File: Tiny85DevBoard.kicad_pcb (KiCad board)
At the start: 2 copper layers, 36.1 x 27.4 mm, 13 parts, among them J1 Screw_Terminal_01x02, J2 AVR-ISP-6, J3 Conn_01x04_Female, J4 Conn_01x04_Female, SW1 SW_SPDT, SW2 Reset, U1 LD1117S33TR_SOT223, U2 ATtiny85-20PU

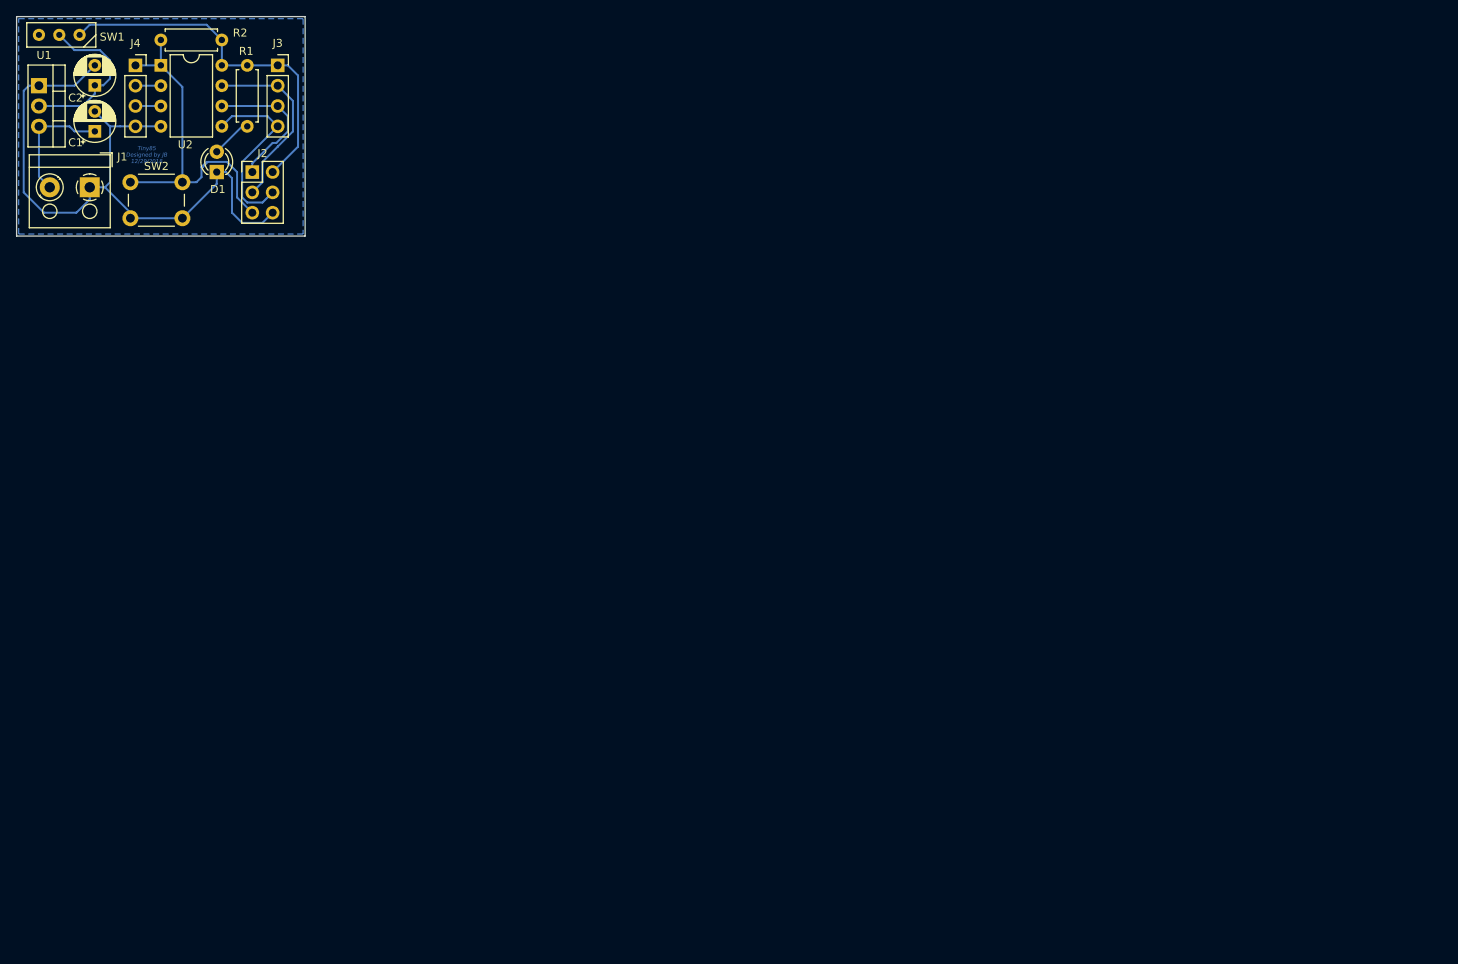
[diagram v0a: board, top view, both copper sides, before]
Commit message: Moved power and added labels.
Moved the power block above the microcontroller and headers so
the headers would be at the sides of the board. Added silkscreen
labels for power, pin names, and header names.
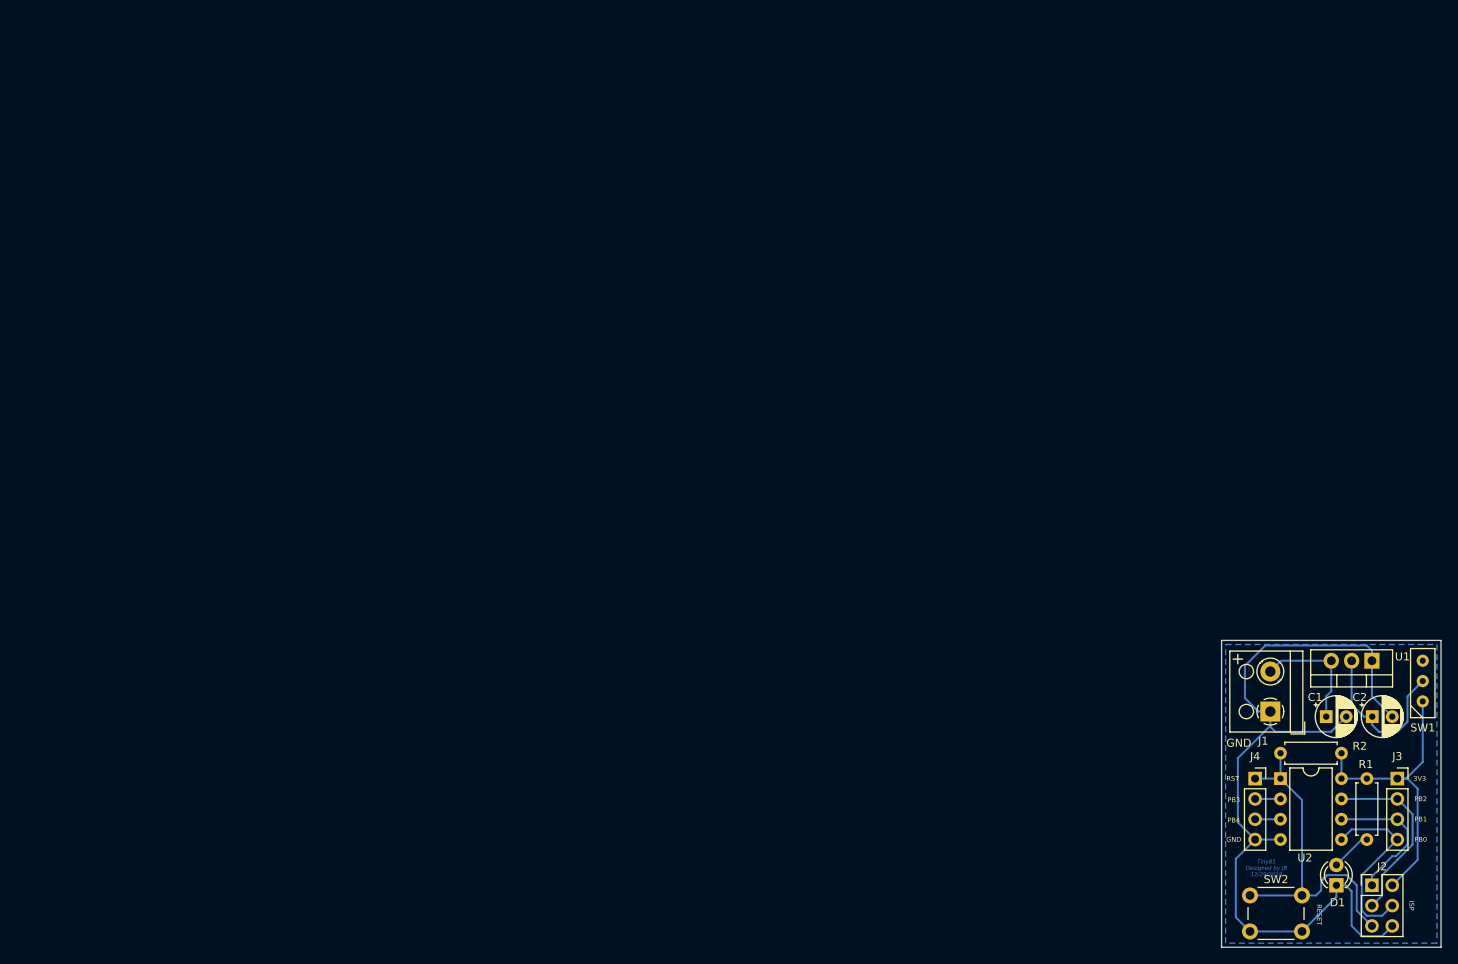
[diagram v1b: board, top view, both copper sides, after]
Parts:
- moved SW1 187.4 mm to (188.2, 98.0), turned to 90 degrees
- moved U1 181.5 mm to (181.9, 93.0), turned to 180 degrees
- moved C2 178.1 mm to (181.9, 99.9), turned to 0 degrees
- moved C1 170.4 mm to (176.1, 99.9), turned to 0 degrees
- moved D1 165.9 mm to (177.4, 121.0)
- moved J2 165.9 mm to (181.9, 121.0)
- moved R1 165.9 mm to (181.2, 107.7)
- moved R2 165.9 mm to (170.4, 104.5)
- moved SW2 165.9 mm to (166.6, 122.3)
- moved U2 165.9 mm to (170.4, 107.7)
- moved J3 165.9 mm to (185.0, 107.7)
- moved J4 165.9 mm to (167.3, 107.7)
- moved J1 161.5 mm to (169.2, 99.3), turned to 90 degrees
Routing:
- net GNDPWR: track 85.1 -> 107.5 mm
- net +3V3: track 45.7 -> 38.2 mm
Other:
- board size 36.1 x 27.4 mm -> 27.4 x 38.4 mm
- board text added: "+"
- board text added: "3V3"
- board text added: "GND"
- board text added: "ISP"
- board text added: "PB0"
- board text added: "PB1"
- board text added: "PB2"
- board text added: "PB3"
- board text added: "PB4"
- board text added: "RESET"
- board text added: "RST"

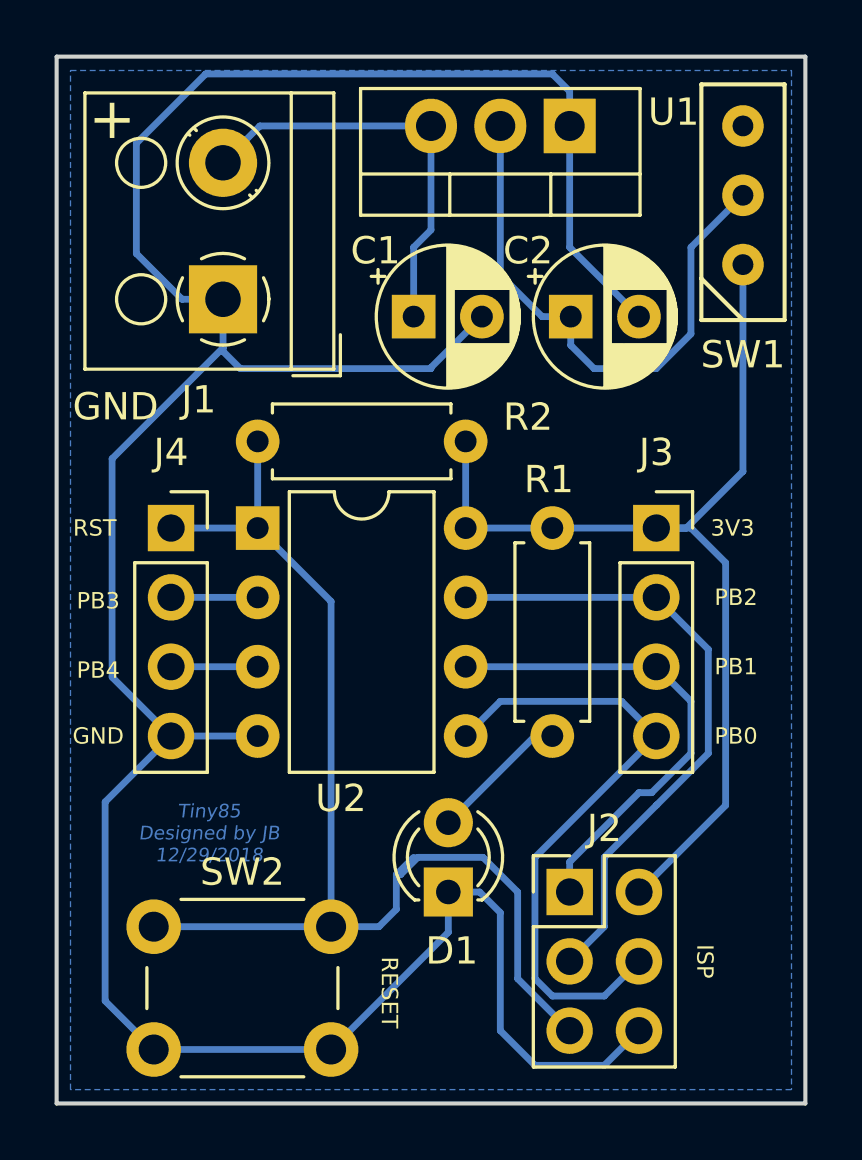
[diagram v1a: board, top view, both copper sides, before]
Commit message: Moved reset switch closer to ATTiny.
There was dead space between the reset switch and the MCU. Moved
the reset switch to eliminate this space.
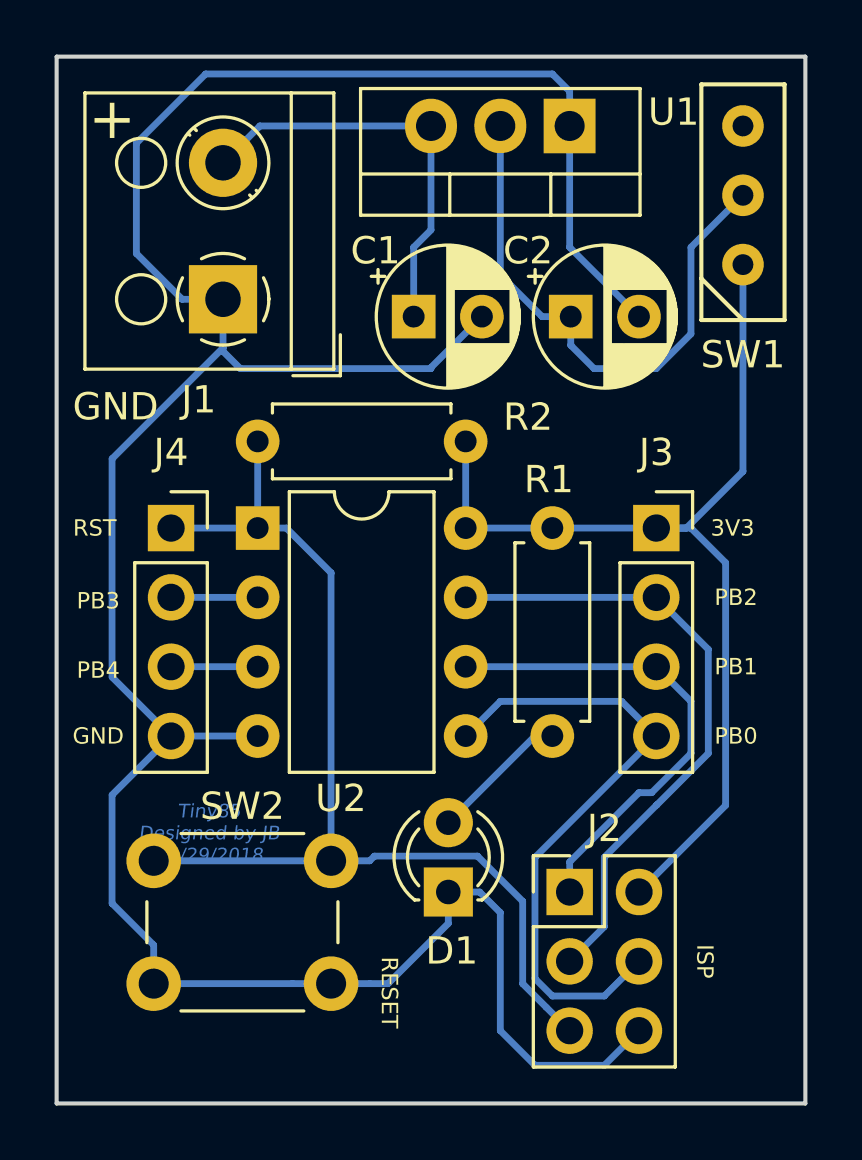
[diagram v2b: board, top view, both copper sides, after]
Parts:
- moved SW2 2.41 mm to (166.6, 119.9)
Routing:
- net GNDPWR: track 107.5 -> 103.0 mm
- net /RESET: track 44.5 -> 40.0 mm
- removed copper zone on B.Cu, net GNDPWR

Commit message: Tightened board, rotated ISP header.
Eliminated dead spaces between components in the power section.
Rotated the ISP header to make it easier to plug in.
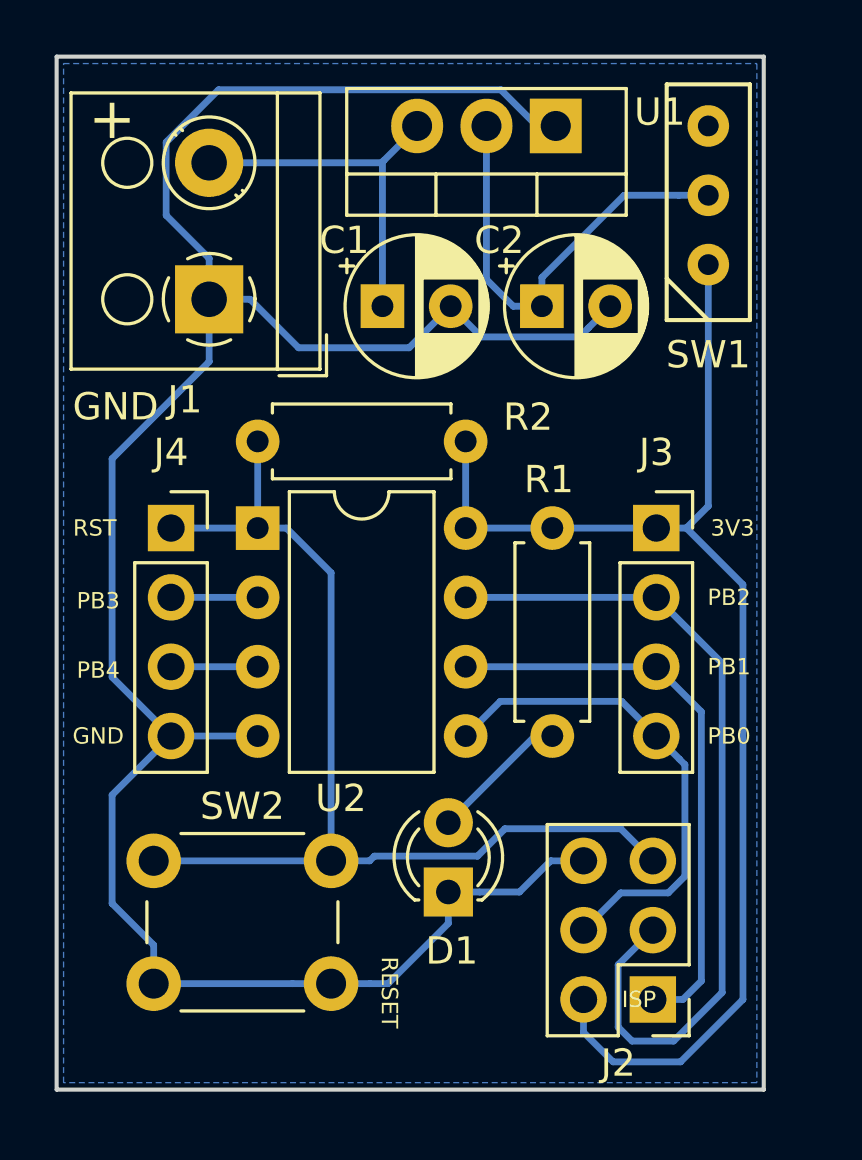
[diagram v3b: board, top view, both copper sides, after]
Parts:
- moved J2 4.98 mm to (184.9, 125.0), turned to 180 degrees
- moved SW1 1.27 mm to (186.9, 98.0)
- moved C1 1.20 mm to (175.0, 99.6)
- moved C2 1.12 mm to (180.8, 99.6)
- moved U1 0.51 mm to (181.4, 93.0)
- moved J1 0.51 mm to (168.7, 99.3)
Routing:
- net GNDPWR: track 103.0 -> 89.4 mm
- net +3V3: track 38.2 -> 47.8 mm
- net /SCK: track 23.2 -> 31.3 mm
- net /MOSI: track 23.4 -> 18.1 mm
- net Net-(C2-Pad1): track 20.9 -> 16.5 mm
- net /MISO: track 17.9 -> 21.2 mm
- net Net-(C1-Pad1): track 15.4 -> 13.6 mm
- added copper zone on B.Cu, net GNDPWR
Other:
- board size 27.4 x 38.4 mm -> 25.9 x 37.8 mm
- board text removed: "Tiny85 Designed by JB 12/29/2018"

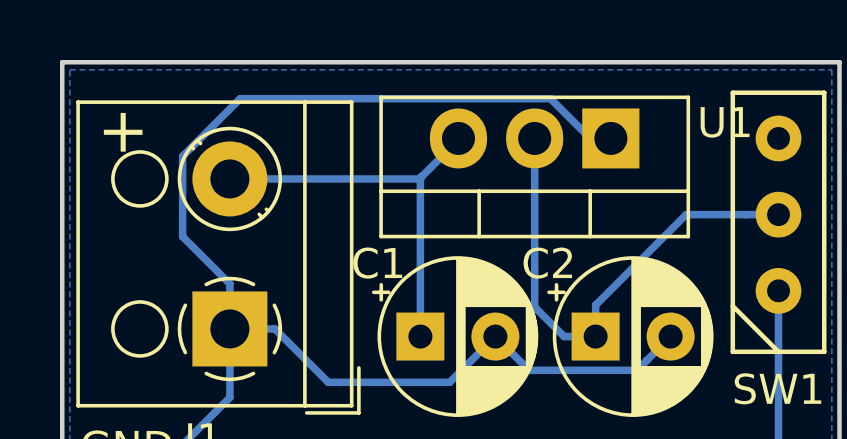
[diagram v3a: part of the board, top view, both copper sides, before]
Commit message: Fine-tuned trace placement.
Moved some ground traces so that they would be within the ground
plane.
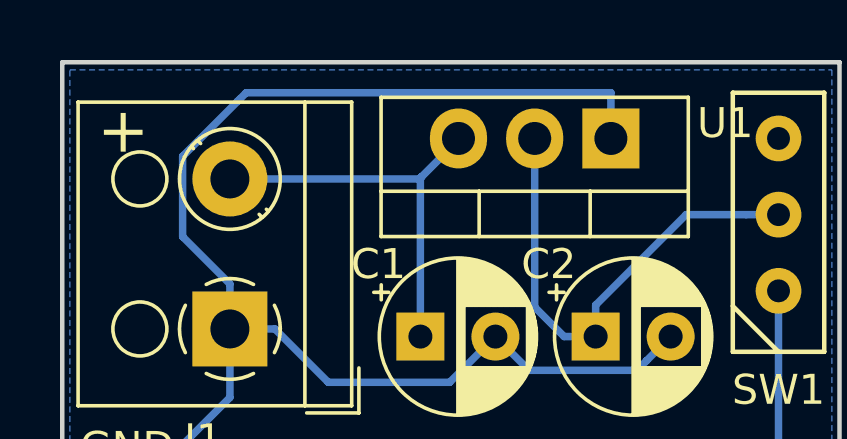
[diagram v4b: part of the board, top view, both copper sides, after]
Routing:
- net GNDPWR: track 89.4 -> 91.3 mm
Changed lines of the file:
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@@
     (thickness 1.6)
     (drawings 16)
-    (tracks 97)
+    (tracks 99)
     (zones 0)
     (modules 13)
@@
     (visible_elements FFFFFF7F)
     (pcbplotparams
-      (layerselection 0x01000_fffffffe)
+      (layerselection 0x01020_fffffffe)
       (usegerberextensions false)
       (usegerberattributes false)
@@
   (segment (start 178.631001 100.693001) (end 182.222999 100.693001) (width 0.25) (layer B.Cu) (net 4))
   (segment (start 177.506 99.568) (end 178.631001 100.693001) (width 0.25) (layer B.Cu) (net 4))
+  (segment (start 181.356 92.964) (end 180.670171 92.964) (width 0.25) (layer B.Cu) (net 4))
+  (segment (start 168.656 97.814) (end 168.656 99.314) (width 0.25) (layer B.Cu) (net 4))
   (segment (start 167.080999 96.238999) (end 168.656 97.814) (width 0.25) (layer B.Cu) (net 4))
-  (segment (start 168.656 97.814) (end 168.656 99.314) (width 0.25) (layer B.Cu) (net 4))
   (segment (start 167.080999 93.557999) (end 167.080999 96.238999) (width 0.25) (layer B.Cu) (net 4))
-  (segment (start 179.345161 91.63899) (end 169.000008 91.63899) (width 0.25) (layer B.Cu) (net 4))
-  (segment (start 180.670171 92.964) (end 179.345161 91.63899) (width 0.25) (layer B.Cu) (net 4))
-  (segment (start 169.000008 91.63899) (end 167.080999 93.557999) (width 0.25) (layer B.Cu) (net 4))
-  (segment (start 181.356 92.964) (end 180.670171 92.964) (width 0.25) (layer B.Cu) (net 4))
+  (segment (start 181.356 92.964) (end 181.356 91.44) (width 0.25) (layer B.Cu) (net 4))
+  (segment (start 181.356 91.44) (end 169.198998 91.44) (width 0.25) (layer B.Cu) (net 4))
+  (segment (start 169.198998 91.44) (end 168.91 91.728998) (width 0.25) (layer B.Cu) (net 4))
+  (segment (start 168.91 91.728998) (end 167.080999 93.557999) (width 0.25) (layer B.Cu) (net 4))
+  (segment (start 169.000008 91.63899) (end 168.91 91.728998) (width 0.25) (layer B.Cu) (net 4))
   (segment (start 176.276 93.0115) (end 176.276 92.964) (width 0.25) (layer B.Cu) (net 5))
   (segment (start 168.656 94.314) (end 174.9735 94.314) (width 0.25) (layer B.Cu) (net 5))
